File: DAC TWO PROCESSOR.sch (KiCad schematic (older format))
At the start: 100 parts, among them J1 CONN_20, J2 CONN_10x2, J3 CONN_10, U1 ADP5070, U10 LT1964-SD, U11 SM78L05, U12 SM79L05, U2 REG113-3.3, U3 XX MHz, U4 ADP7118, U5 AT25160B, U6 ADP7182, U7 STM32F7xx, U8 LT1763CS8, U9 LT1763CS8

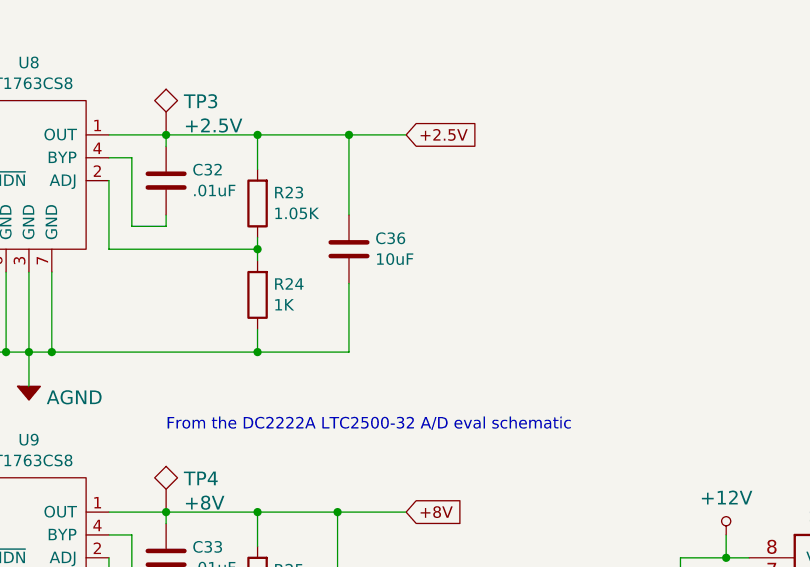
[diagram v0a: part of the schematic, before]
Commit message: Moved cap for demo
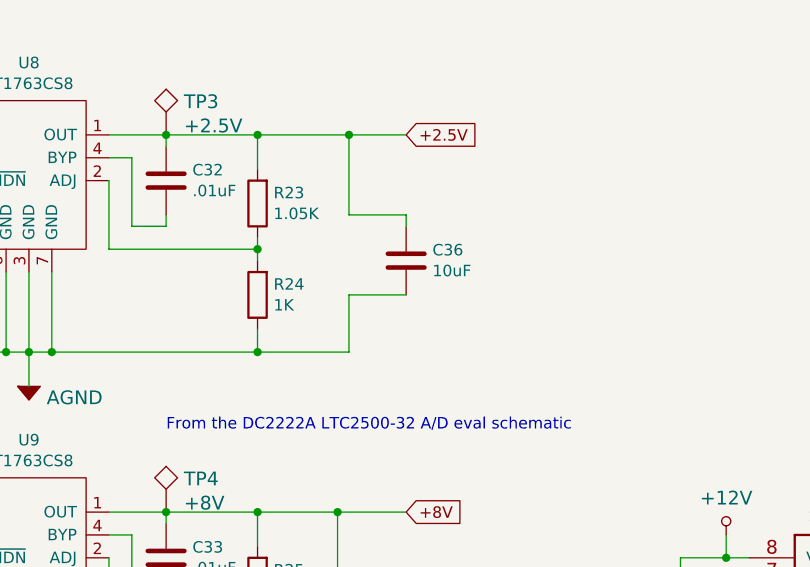
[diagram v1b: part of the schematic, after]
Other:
- moved on the sheet: C36
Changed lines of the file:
@@
 	10550 6250 10950 6250
-Wire Wire Line
-	10950 6900 10950 7200
 Wire Wire Line
 	10950 7200 10550 7200
@@
 L Device:C C36
 U 1 1 5DEA713E
-P 10950 6750
-F 0 "C36" H 11065 6796 50  0000 L CNN
-F 1 "10uF" H 11065 6705 50  0000 L CNN
-F 2 "SciMod:EIA0805" H 10988 6600 50  0001 C CNN
-F 3 "~" H 10950 6750 50  0001 C CNN
-F 4 "GRM21BR71A106KA73K" H 10950 6750 50  0001 C CNN "MANF#"
-	1    10950 6750
+P 11200 6800
+F 0 "C36" H 11315 6846 50  0000 L CNN
+F 1 "10uF" H 11315 6755 50  0000 L CNN
+F 2 "SciMod:EIA0805" H 11238 6650 50  0001 C CNN
+F 3 "~" H 11200 6800 50  0001 C CNN
+F 4 "GRM21BR71A106KA73K" H 11200 6800 50  0001 C CNN "MANF#"
+	1    11200 6800
 	1    0    0    -1
 $EndComp
@@
 F1 "DAC2 ANALOG.sch" 50
 $EndSheet
+Wire Wire Line
+	11200 6650 11200 6600
+Wire Wire Line
+	11200 6600 10950 6600
+Wire Wire Line
+	11200 6950 10950 6950
+Wire Wire Line
+	10950 6950 10950 7200
 $EndSCHEMATC
